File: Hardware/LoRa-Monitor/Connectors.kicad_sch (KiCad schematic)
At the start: 0 parts

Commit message: Finished Energy Meter Module, started LoRa Module and MCU.
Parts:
- added J1: USB_C_Receptacle_USB2.0_16P, Connector_USB:USB_C_Receptacle_HRO_TYPE-C-31-M-12, symbol Connector:USB_C_Receptacle_USB2.0_16P
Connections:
- new net: J1.A1 (GND), J1.A12 (GND), J1.B1 (GND), J1.B12 (GND)
- new net: J1.A4 (VBUS), J1.A9 (VBUS), J1.B4 (VBUS), J1.B9 (VBUS)
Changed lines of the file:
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@@
 	(generator_version "10.0")
 	(paper "A4")
+	(symbol
+		(lib_id "Connector:USB_C_Receptacle_USB2.0_16P")
+		(at 187.96 71.12 0)
+		(unit 1)
+		(body_style 1)
+		(exclude_from_sim no)
+		(in_bom yes)
+		(on_board yes)
+		(in_pos_files yes)
+		(dnp no)
+		(fields_autoplaced yes)
+		(property "Reference" "J1"
+			(at 187.96 48.26 0)
+			(show_name no)
+			(do_not_autoplace no)
+			(effects
+				(font
+					(size 1.27 1.27)
+				)
+			)
+		)
+		(property "Value" "USB_C_Receptacle_USB2.0_16P"
+			(at 187.96 50.8 0)
+			(show_name no)
+			(do_not_autoplace no)
+			(effects
+				(font
+					(size 1.27 1.27)
+				)
+			)
+		)
+		(property "Footprint" "Connector_USB:USB_C_Receptacle_HRO_TYPE-C-31-M-12"
+			(at 191.77 71.12 0)
+			(hide yes)
+			(show_name no)
+			(do_not_autoplace no)
+			(effects
+				(font
+					(size 1.27 1.27)
+				)
+			)
+		)
+		(property "Datasheet" "https://www.usb.org/sites/default/files/documents/usb_type-c.zip"
+			(at 191.77 71.12 0)
+			(hide yes)
+			(show_name no)
+			(do_not_autoplace no)
+			(effects
+				(font
+					(size 1.27 1.27)
+				)
+			)
+		)
+		(property "Description" "USB 2.0-only 16P Type-C Receptacle connector"
+			(at 187.96 71.12 0)
+			(hide yes)
+			(show_name no)
+			(do_not_autoplace no)
+			(effects
+				(font
+					(size 1.27 1.27)
+				)
+			)
+		)
+		(pin "B9"
+		)
+		(pin "B7"
+		)
+		(pin "A12"
+		)
+		(pin "B8"
+		)
+		(pin "A4"
+		)
+		(pin "B12"
+		)
+		(pin "A6"
+		)
+		(pin "A7"
+		)
+		(pin "A8"
+		)
+		(pin "A9"
+		)
+		(pin "SH"
+		)
+		(pin "A5"
+		)
+		(pin "B1"
+		)
+		(pin "A1"
+		)
+		(pin "B4"
+		)
+		(pin "B5"
+		)
+		(pin "B6"
+		)
+		(instances
+			(project "LoRa-Monitor"
+				(path "/7510cc7d-c141-46d4-8947-7def3af8cf35/b9106b62-0c4d-45f8-8fff-77bde9d1c249"
+					(reference "J1")
+					(unit 1)
+				)
+			)
+		)
+	)
 )

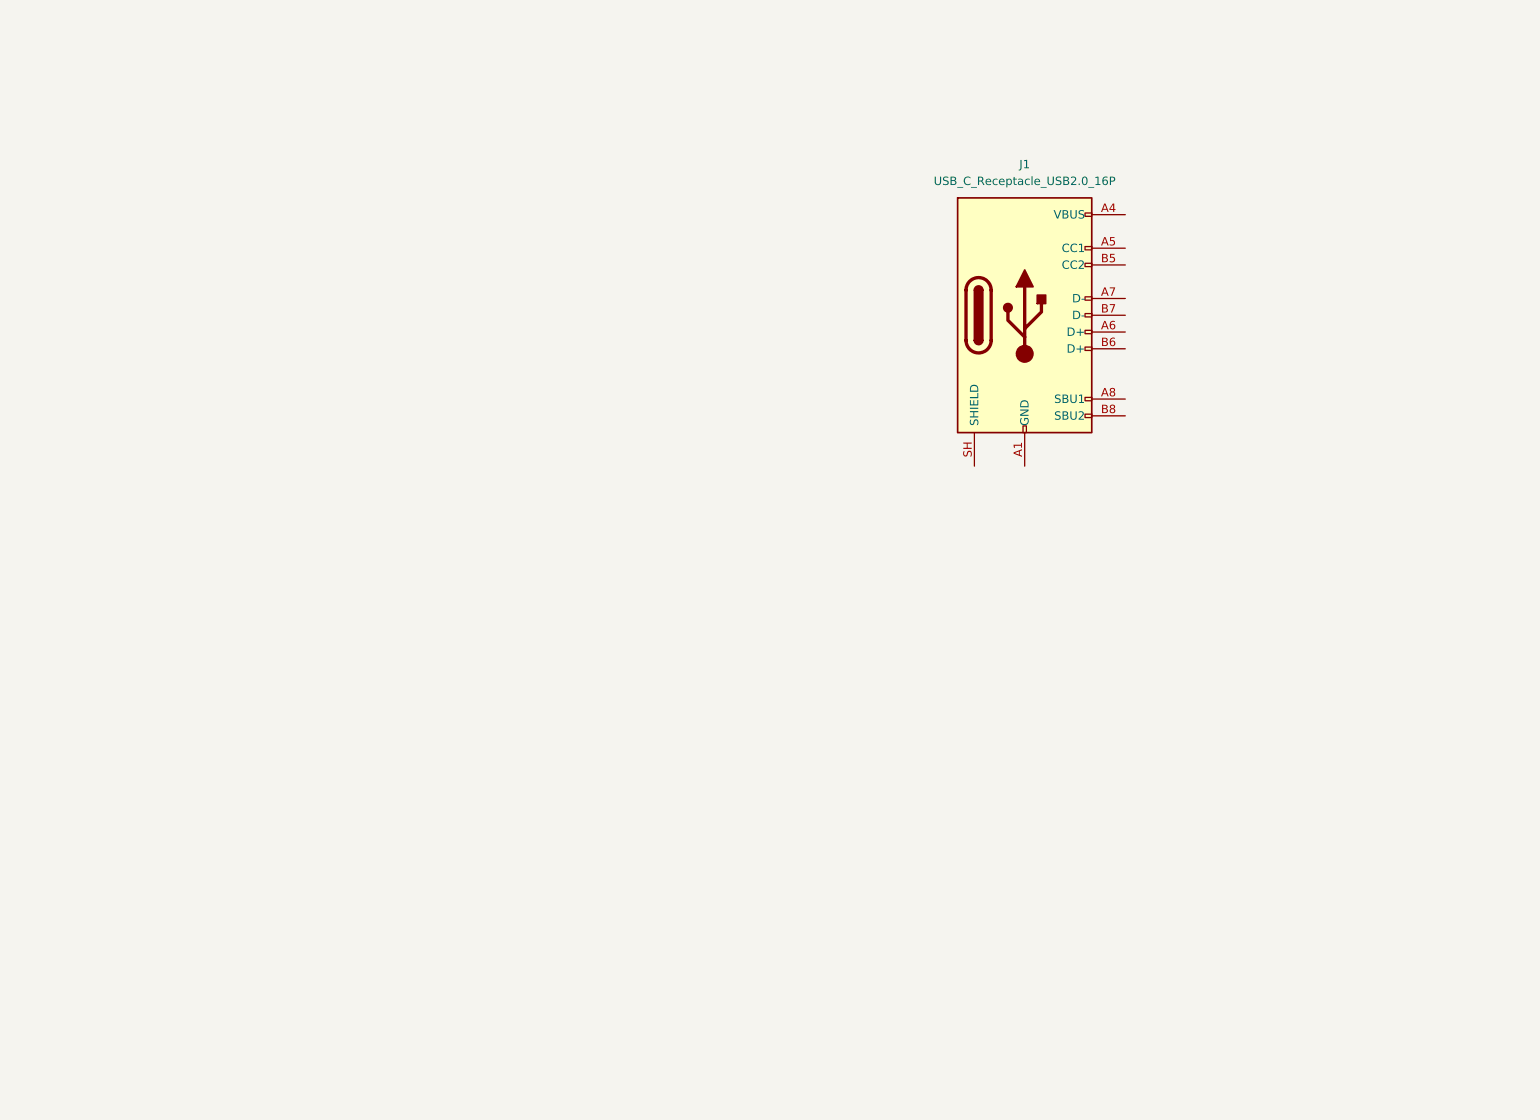
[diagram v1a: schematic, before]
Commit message: Finished MCU and Lora modules. Finished Connectors sheet
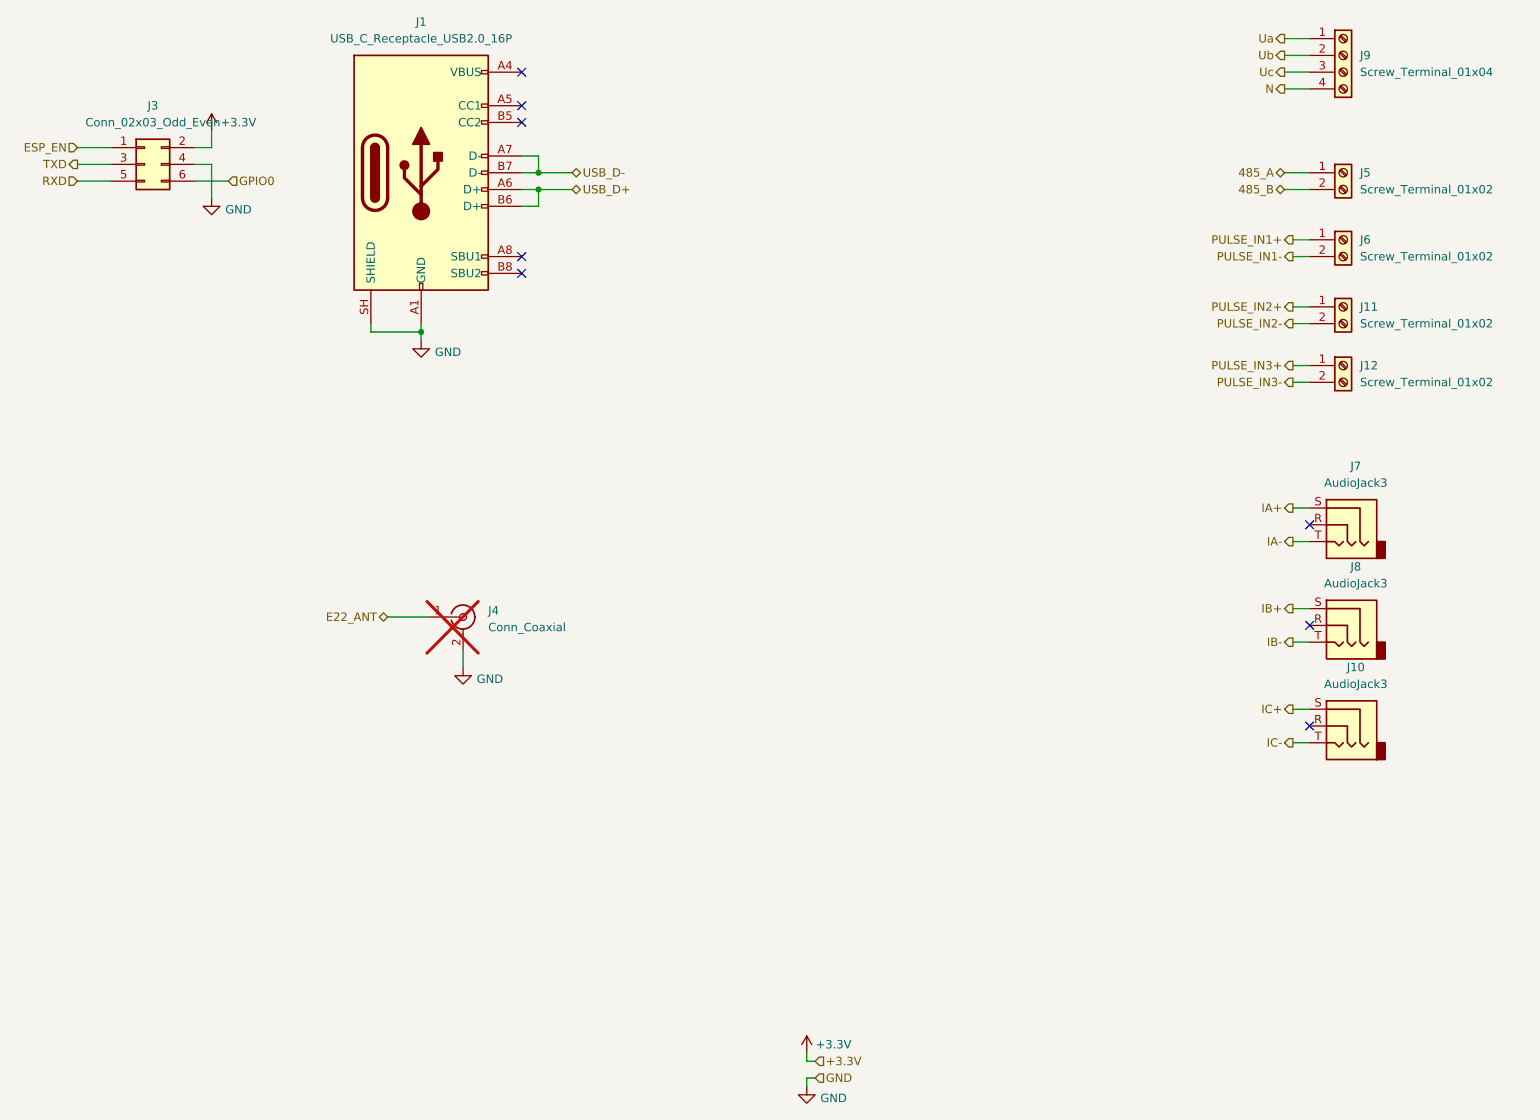
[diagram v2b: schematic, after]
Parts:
- added J10, J7, J8: AudioJack3, Connector_Audio:Jack_3.5mm_CUI_SJ1-3523N_Horizontal, symbol Connector_Audio:AudioJack3
- added J11, J12, J5, J6: Screw_Terminal_01x02, TerminalBlock_Phoenix:TerminalBlock_Phoenix_PT-1,5-2-5.0-H_1x02_P5.00mm_Horizontal, symbol Connector:Screw_Terminal_01x02
- added J3: Conn_02x03_Odd_Even, Connector_PinHeader_2.54mm:PinHeader_2x03_P2.54mm_Vertical, symbol Connector_Generic:Conn_02x03_Odd_Even
- added J4: Conn_Coaxial, Connector_Coaxial:SMA_Amphenol_901-144_Vertical, symbol Connector:Conn_Coaxial
- added J9: Screw_Terminal_01x04, TerminalBlock_Phoenix:TerminalBlock_Phoenix_PT-1,5-4-5.0-H_1x04_P5.00mm_Horizontal, symbol Connector:Screw_Terminal_01x04
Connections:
- net GND: now reaches J1.A1 (GND), J1.A12 (GND), J1.B1 (GND), J1.B12 (GND)
- net GND: now also J1.SH (SHIELD), J3.4 (Pin_4), J4.2 (Ext)
- net USB_D+: now reaches J1.A6 (D+)
- net USB_D+: now also J1.B6 (D+)
- net USB_D-: now reaches J1.A7 (D-)
- net USB_D-: now also J1.B7 (D-)
- new net +3.3V: J3.2 (Pin_2)
- new net 485_A: J5.1 (Pin_1)
- new net 485_B: J5.2 (Pin_2)
- new net E22_ANT: J4.1 (In)
- new net ESP_EN: J3.1 (Pin_1)
- new net GPIO0: J3.6 (Pin_6)
- new net IA+: J7.S
- new net IA-: J7.T
- new net IB+: J8.S
- new net IB-: J8.T
- new net IC+: J10.S
- new net IC-: J10.T
- new net N: J9.4 (Pin_4)
- new net PULSE_IN1+: J6.1 (Pin_1)
- new net PULSE_IN1-: J6.2 (Pin_2)
- new net PULSE_IN2+: J11.1 (Pin_1)
- new net PULSE_IN2-: J11.2 (Pin_2)
- new net PULSE_IN3+: J12.1 (Pin_1)
- new net PULSE_IN3-: J12.2 (Pin_2)
- new net RXD: J3.5 (Pin_5)
- new net TXD: J3.3 (Pin_3)
- new net Ua: J9.1 (Pin_1)
- new net Ub: J9.2 (Pin_2)
- new net Uc: J9.3 (Pin_3)
- no-connect marks 0 -> 8
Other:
- moved on the sheet: J1

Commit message: Finished schematic, started with PCB design
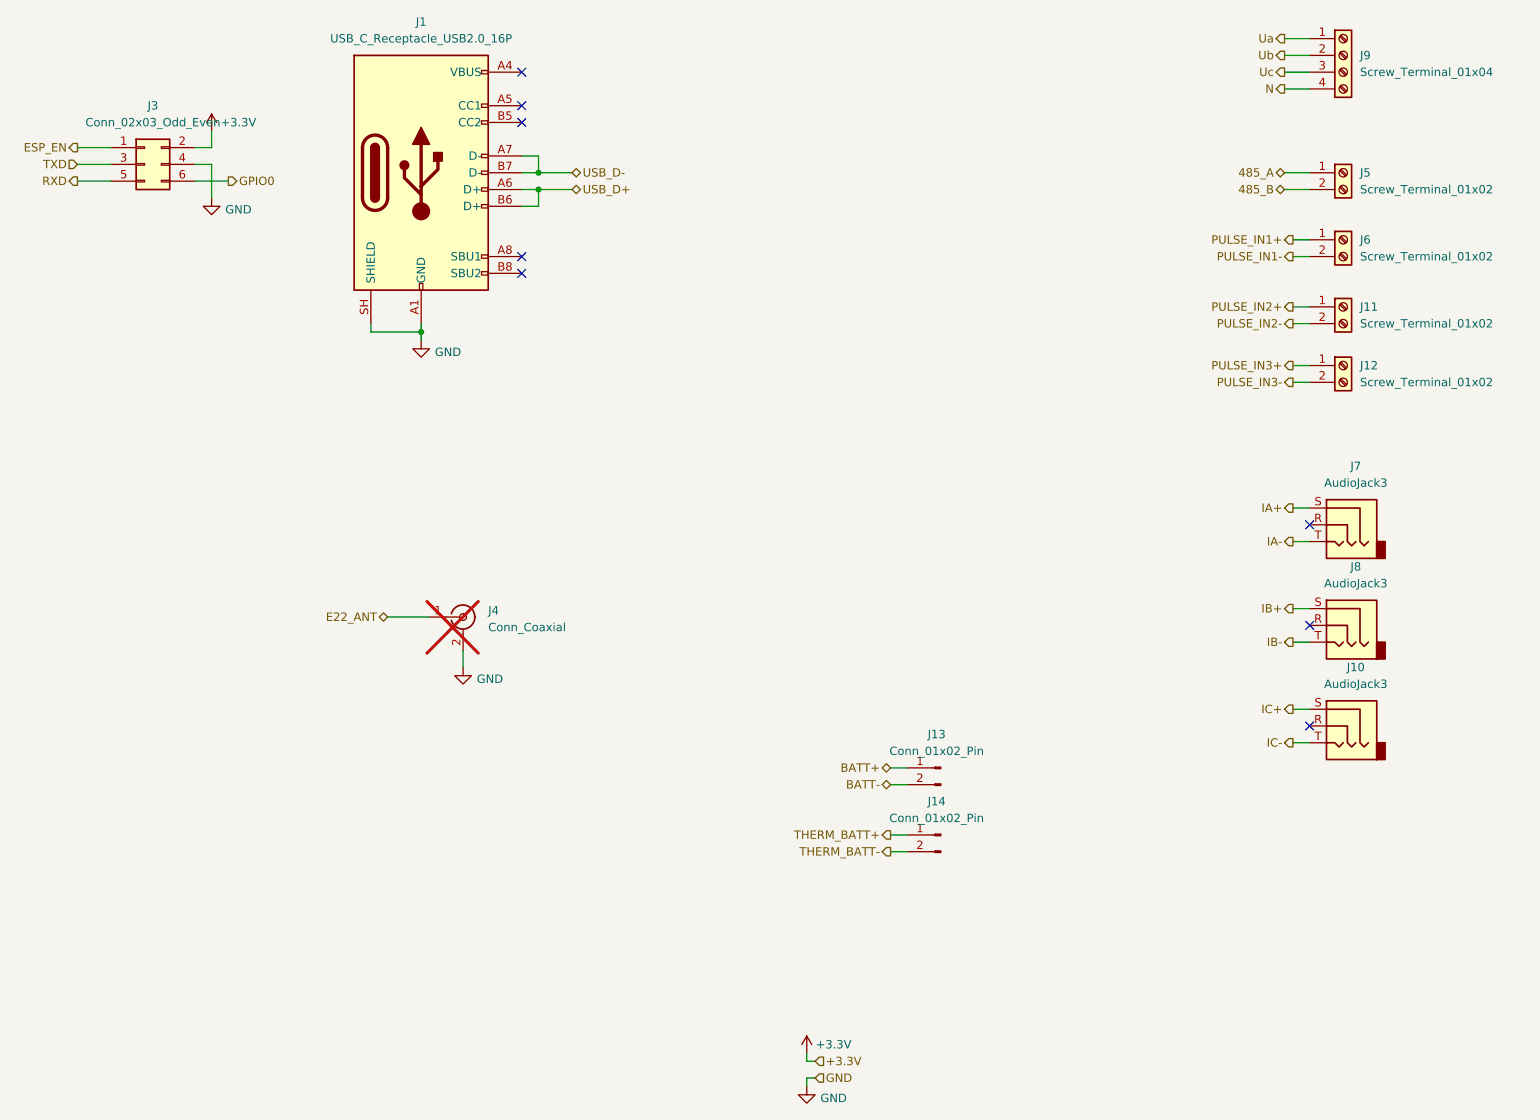
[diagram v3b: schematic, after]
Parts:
- added J13, J14: Conn_01x02_Pin, Connector_JST:JST_PH_B2B-PH-K_1x02_P2.00mm_Vertical, symbol Connector:Conn_01x02_Pin
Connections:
- new net BATT+: J13.1 (Pin_1)
- new net BATT-: J13.2 (Pin_2)
- new net THERM_BATT+: J14.1 (Pin_1)
- new net THERM_BATT-: J14.2 (Pin_2)
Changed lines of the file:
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@@
+	(wire
+		(pts
+			(xy 167.64 149.86) (xy 170.18 149.86)
+		)
+		(stroke
+			(width 0)
+			(type default)
+		)
+	)
 	(wire
 		(pts
@@
 	(wire
 		(pts
+			(xy 167.64 139.7) (xy 170.18 139.7)
+		)
+		(stroke
+			(width 0)
+			(type default)
+		)
+	)
+	(wire
+		(pts
 			(xy 111.76 54.61) (xy 114.3 54.61)
 		)
@@
 	(wire
 		(pts
+			(xy 167.64 152.4) (xy 170.18 152.4)
+		)
+		(stroke
+			(width 0)
+			(type default)
+		)
+	)
+	(wire
+		(pts
 			(xy 228.6 120.65) (xy 231.14 120.65)
 		)
@@
 	(wire
 		(pts
+			(xy 167.64 142.24) (xy 170.18 142.24)
+		)
+		(stroke
+			(width 0)
+			(type default)
+		)
+	)
+	(wire
+		(pts
 			(xy 228.6 130.81) (xy 231.14 130.81)
 		)
@@
 	)
 	(hierarchical_label "TXD"
-		(shape output)
+		(shape input)
 		(at 44.45 48.26 180)
 		(effects
@@
 		(shape output)
 		(at 227.33 29.21 180)
+		(effects
+			(font
+				(size 1.27 1.27)
+			)
+			(justify right)
+		)
+	)
+	(hierarchical_label "THERM_BATT-"
+		(shape output)
+		(at 167.64 152.4 180)
 		(effects
 			(font
@@
 		)
 	)
+	(hierarchical_label "BATT-"
+		(shape bidirectional)
+		(at 167.64 142.24 180)
+		(effects
+			(font
+				(size 1.27 1.27)
+			)
+			(justify right)
+		)
+	)
 	(hierarchical_label "485_B"
 		(shape bidirectional)
@@
 	)
 	(hierarchical_label "RXD"
-		(shape input)
+		(shape output)
 		(at 44.45 50.8 180)
 		(effects
@@
 		(shape output)
 		(at 227.33 36.83 180)
+		(effects
+			(font
+				(size 1.27 1.27)
+			)
+			(justify right)
+		)
+	)
+	(hierarchical_label "BATT+"
+		(shape bidirectional)
+		(at 167.64 139.7 180)
+		(effects
+			(font
+				(size 1.27 1.27)
+			)
+			(justify right)
+		)
+	)
+	(hierarchical_label "THERM_BATT+"
+		(shape output)
+		(at 167.64 149.86 180)
 		(effects
 			(font
@@
 	)
 	(hierarchical_label "ESP_EN"
-		(shape input)
+		(shape output)
 		(at 44.45 45.72 180)
 		(effects
@@
 	)
 	(hierarchical_label "GPIO0"
-		(shape input)
+		(shape output)
 		(at 67.31 50.8 0)
 		(effects
@@
 	)
 	(symbol
+		(lib_id "Connector:Conn_01x02_Pin")
+		(at 175.26 139.7 0)
+		(mirror y)
+		(unit 1)
+		(body_style 1)
+		(exclude_from_sim no)
+		(in_bom yes)
+		(on_board yes)
+		(in_pos_files yes)
+		(dnp no)
+		(fields_autoplaced yes)
+		(property "Reference" "J13"
+			(at 174.625 134.62 0)
+			(show_name no)
+			(do_not_autoplace no)
+			(effects
+				(font
+					(size 1.27 1.27)
+				)
+			)
+		)
+		(property "Value" "Conn_01x02_Pin"
+			(at 174.625 137.16 0)
+			(show_name no)
+			(do_not_autoplace no)
+			(effects
+				(font
+					(size 1.27 1.27)
+				)
+			)
+		)
+		(property "Footprint" "Connector_JST:JST_PH_B2B-PH-K_1x02_P2.00mm_Vertical"
+			(at 175.26 139.7 0)
+			(hide yes)
+			(show_name no)
+			(do_not_autoplace no)
+			(effects
+				(font
+					(size 1.27 1.27)
+				)
+			)
+		)
+		(property "Datasheet" ""
+			(at 175.26 139.7 0)
+			(hide yes)
+			(show_name no)
+			(do_not_autoplace no)
+			(effects
+				(font
+					(size 1.27 1.27)
+				)
+			)
+		)
+		(property "Description" "Generic connector, single row, 01x02, script generated"
+			(at 175.26 139.7 0)
+			(hide yes)
+			(show_name no)
+			(do_not_autoplace no)
+			(effects
+				(font
+					(size 1.27 1.27)
+				)
+			)
+		)
+		(pin "2"
+		)
+		(pin "1"
+		)
+		(instances
+			(project "LoRa-Monitor"
+				(path "/7510cc7d-c141-46d4-8947-7def3af8cf35/b9106b62-0c4d-45f8-8fff-77bde9d1c249"
+					(reference "J13")
+					(unit 1)
+				)
+			)
+		)
+	)
+	(symbol
 		(lib_id "Connector_Audio:AudioJack3")
 		(at 236.22 118.11 0)
@@
 					(unit 1)
 				)
+			)
+		)
+	)
+	(symbol
+		(lib_id "Connector:Conn_01x02_Pin")
+		(at 175.26 149.86 0)
+		(mirror y)
+		(unit 1)
+		(body_style 1)
+		(exclude_from_sim no)
+		(in_bom yes)
+		(on_board yes)
+		(in_pos_files yes)
+		(dnp no)
+		(fields_autoplaced yes)
+		(property "Reference" "J14"
+			(at 174.625 144.78 0)
+			(show_name no)
+			(do_not_autoplace no)
+			(effects
+				(font
+					(size 1.27 1.27)
+				)
+			)
+		)
+		(property "Value" "Conn_01x02_Pin"
+			(at 174.625 147.32 0)
+			(show_name no)
+			(do_not_autoplace no)
+			(effects
+				(font
+					(size 1.27 1.27)
+				)
+			)
+		)
+		(property "Footprint" "Connector_JST:JST_PH_B2B-PH-K_1x02_P2.00mm_Vertical"
+			(at 175.26 149.86 0)
+			(hide yes)
+			(show_name no)
+			(do_not_autoplace no)
+			(effects
+				(font
+					(size 1.27 1.27)
+				)
+			)
+		)
+		(property "Datasheet" ""
+			(at 175.26 149.86 0)
+			(hide yes)
+			(show_name no)
+			(do_not_autoplace no)
+			(effects
+				(font
+					(size 1.27 1.27)
+				)
+			)
+		)
+		(property "Description" "Generic connector, single row, 01x02, script generated"
+			(at 175.26 149.86 0)
+			(hide yes)
+			(show_name no)
+			(do_not_autoplace no)
+			(effects
+				(font
+					(size 1.27 1.27)
+				)
+			)
+		)
+		(pin "2"
+		)
+		(pin "1"
+		)
+		(instances
+			(project "LoRa-Monitor"
+				(path "/7510cc7d-c141-46d4-8947-7def3af8cf35/b9106b62-0c4d-45f8-8fff-77bde9d1c249"
+					(reference "J14")
+					(unit 1)
+				)

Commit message: Started routing.
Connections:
- net Ua: now also J9.3 (Pin_3); no longer J9.1 (Pin_1)
- net Uc: now also J9.1 (Pin_1); no longer J9.3 (Pin_3)
